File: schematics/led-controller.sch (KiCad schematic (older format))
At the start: 58 parts, among them IC1 ATMEGA168A-P, P1 CONN_01X03, P2 CONN_01X03, P3 CONN_01X02, P4 CONN_01X02, P5 CONN_01X02, P6 CONN_01X02, P7 ISP, P8 COM, Q1 IRLU 120N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

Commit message: first checked version
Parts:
- removed JP1: Jumper_NO_Small, Pin_Headers:Pin_Header_Straight_1x02, symbol Jumper_NO_Small
- added C10, C11: 100n, Capacitors_ThroughHole:C_Rect_L7_W2.5_P5, symbol C
- added CON1: BARREL_JACK, Connect:BARREL_JACK, symbol BARREL_JACK
- added D6: 1N5408, Diodes_ThroughHole:Diode_DO-201AD_Horizontal_RM15, symbol D
- added F1: 3A, Fuse_Holders_and_Fuses:Fuseholder5x20_horiz_open_lateral_Type-II, symbol FUSE
- added unit 6 of U2
- added unit 5 of U2
- C1, C2, C3, C4: footprint Capacitors_ThroughHole:C_Radial_D5_L11_P2.5 -> Capacitors_ThroughHole:C_Radial_D8_L11.5_P3.5; Order (none) -> RAD FR 100/35; Price (none) -> 0,21
- C5, C6, C7, C8, C9: Order (none) -> MKS2-100 100N; Price (none) -> 0.09
- P1: value CONN_01X03 -> VIN
- P2: value CONN_01X03 -> VOUT
- P3: value CONN_01X02 -> LED1; footprint Connect:AK300-2 -> Connect:bornier2
- P4, P5, P6: footprint Connect:AK300-2 -> Connect:bornier2
- P7: footprint Socket_Strips:Socket_Strip_Straight_2x03 -> Pin_Headers:Pin_Header_Straight_2x03
- RR4: value 20k -> 27k; Order (none) -> SIL 5-4 27; Price (none) -> 0.06
- RV1, RV2, RV3, RV4: footprint Potentiometers:Potentiometer_Trimmer-Suntan-TSR-3386C -> Trimmers:Potentiometer_Trimmer-Suntan-TSR-3296; Order (none) -> 64W-10K; Price (none) -> 0.32
- U2: footprint Housings_DIP:DIP-14_W7.62mm -> (none)
- U3: value LF33CV -> LP 2950 ACZ3,3; footprint TO_SOT_Packages_THT:TO-220_Neutral123_Vertical -> TO_SOT_Packages_THT:TO-92_Inline_Narrow_Oval; Order (none) -> LP 2950 ACZ3,3; Price (none) -> 0.33
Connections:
- net +3V3: now also P1.2 (P2), P2.2 (P2), C10.1, C11.1, U2.14 (+3V3), U2.14 (+3V3); no longer C6.1, C7.1
- net GND: now also U2.1, U2.3, C10.2, C11.2, CON1.2, CON1.3, U2.7 (GND), U2.7 (GND)
- net IRAW1: now also P3.2 (P2); no longer P3.1 (P1)
- net IRAW2: now also P4.2 (P2); no longer P4.1 (P1)
- net IRAW3: now also P5.2 (P2); no longer P5.1 (P1)
- net IRAW4: now also P6.2 (P2); no longer P6.1 (P1)
- net PULLUP1: now also RR3.3, U2.11; no longer RR3.2, U2.1
- net PULLUP2: now also RR3.2, U2.13; no longer RR3.3, U2.3
- net PULLUP3: now also RR3.5; no longer RR3.4
- net PULLUP4: now also RR3.4; no longer RR3.5
- net SENSE1: now also IC1.25 ((PCINT10/ADC2)PC2), U2.10; no longer IC1.26 ((PCINT11/ADC3)PC3), U2.2
- net SENSE2: now also IC1.26 ((PCINT11/ADC3)PC3), U2.12; no longer IC1.25 ((PCINT10/ADC2)PC2), U2.4
- net VCC: now also C6.1, C7.1, D6.1 (K)
- net at L1.1: now also P3.1 (P1); no longer P3.2 (P2)
- net at L2.1: now also P4.1 (P1); no longer P4.2 (P2)
- net at L3.1: now also P5.1 (P1); no longer P5.2 (P2)
- net at L4.1: now also P6.1 (P1); no longer P6.2 (P2)
- new net: CON1.1, F1.1
- new net: D6.2 (A), F1.2
- no-connect marks 12 -> 14
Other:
- moved on the sheet: C5, P3, P4, P5, P6, U3

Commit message: Board version 1.0 RC1
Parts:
- removed D1: 3V6, Discret:D4, symbol ZENER
- removed D6: 1N5408, Diodes_ThroughHole:Diode_DO-201AD_Horizontal_RM15, symbol D
- removed R1: 1k, Resistors_ThroughHole:Resistor_Horizontal_RM10mm, symbol R
- added C12, C13: 100n, Capacitors_ThroughHole:C_Rect_L7_W2.5_P5, symbol C
- added P9: EXPANSION, Pin_Headers:Pin_Header_Straight_1x04, symbol CONN_01X04
- added U5: 7905_wno, TO_SOT_Packages_THT:TO-92_Inline_Narrow_Oval, symbol 7905_wno
- D2, D3, D4, D5: value SD101C -> 1N5819
- P1, P2, P8: footprint Pin_Headers:Pin_Header_Straight_1x03 -> Connect:PINHEAD1-3
- R14, R15, R16: footprint Resistors_ThroughHole:Resistor_Horizontal_RM10mm -> Discret:R1
- RP1, RP2, RR1, RR2, RR3: value 10k -> 100k
- RR4: value 27k -> 4.7k; Order SIL 5-4 27 -> SIL 5-4 4,7K
- RV1, RV2, RV3, RV4: value 10k -> 1k; Order 64W-10K -> 64W-1K
- U2: footprint (none) -> Housings_DIP:DIP-14_W7.62mm
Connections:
- net +3V3: now also IC1.20 (AVCC), R14.2; no longer R14.1
- net GND: now also C13.2, U5.2 (VI)
- net ISENSE1: now also U1.4 (-); no longer U1.5 (+)
- net ISENSE2: now also U1.6 (-); no longer U1.7 (+)
- net ISENSE3: now also U1.10 (-); no longer U1.11 (+)
- net ISENSE4: now also U1.8 (-); no longer U1.9 (+)
- net REF1: now also U1.5 (+); no longer U1.4 (-)
- net REF2: now also U1.7 (+); no longer U1.6 (-)
- net REF3: now also U1.11 (+); no longer U1.10 (-)
- net REF4: now also U1.9 (+); no longer U1.8 (-)
- net RESET: now also R14.1; no longer R14.2
- net VCC: now also F1.2, C12.2, U5.1 (GND)
- net at IC1.21 (AREF): now also C13.1
- net E4: now reaches IC1.27 ((PCINT12/SDA/ADC4)PC4)
- net E4: now also P9.4 (P4)
- net E2: now reaches IC1.28 ((PCINT13/SCL/ADC5)PC5)
- net E2: now also P9.2 (P2)
- net E1: now reaches IC1.4 ((PCINT18/INT0)PD2)
- net E1: now also P9.1 (P1)
- net E3: now reaches IC1.5 ((PCINT19/OC2B/INT1)PD3)
- net E3: now also P9.3 (P3)
- net -5V: now reaches RR4.1 (COM)
- net -5V: now also C12.1, U5.3 (VO)
- no-connect marks 14 -> 8
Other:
- moved on the sheet: RP1, RR1, RR4, RV1, RV2, RV3, RV4

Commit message: Led Controller RC2
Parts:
- added C14, C15: 1u, Capacitors_ThroughHole:C_Radial_D5_L6_P2.5, symbol CP
- RP1, RP2: footprint Pin_Headers:Pin_Header_Straight_1x08 -> w_pth_resistors:r-sil_8
- RR1, RR2, RR3, RR4: footprint Pin_Headers:Pin_Header_Straight_1x05 -> w_pth_resistors:r-sil_5
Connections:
- net +3V3: now also C14.1
- net -5V: now also C15.2
- net GND: now also C14.2
- net VCC: now also C15.1
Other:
- moved on the sheet: C1, C10, C11, C2, C3, C4, C5, C6, C7, C8, C9, U3

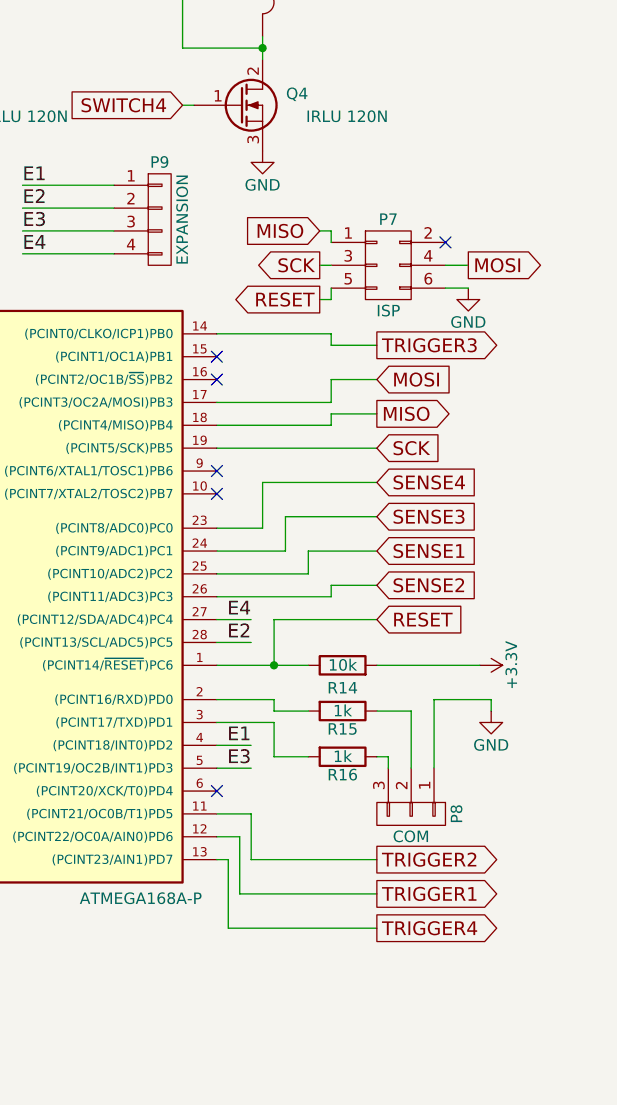
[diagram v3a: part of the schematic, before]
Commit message: RC3 -- Connected all pins to PWM outputs
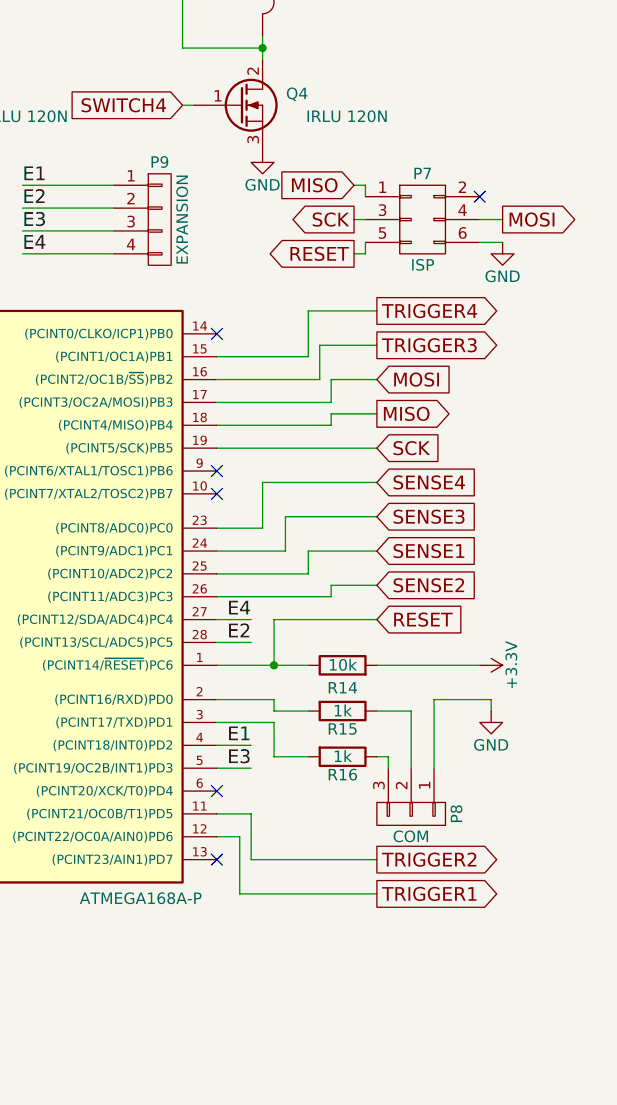
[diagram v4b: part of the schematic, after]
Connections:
- net TRIGGER3: now also IC1.16 ((PCINT2/OC1B/~SS~)PB2); no longer IC1.14 ((PCINT0/CLKO/ICP1)PB0)
- net TRIGGER4: now also IC1.15 ((PCINT1/OC1A)PB1); no longer IC1.13 ((PCINT23/AIN1)PD7)
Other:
- moved on the sheet: P7
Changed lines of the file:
@@
 Text GLabel 10400 4800 2    60   Input ~ 0
 SENSE2
-Text GLabel 10400 6300 2    60   Output ~ 0
+Text GLabel 10400 3600 2    60   Output ~ 0
 TRIGGER4
 Text GLabel 10400 6150 2    60   Output ~ 0
@@
 L CONN_02X03 P7
 U 1 1 5817965E
-P 10450 3400
-F 0 "P7" H 10450 3600 50  0000 C CNN
-F 1 "ISP" H 10450 3200 50  0000 C CNN
-F 2 "Pin_Headers:Pin_Header_Straight_2x03" H 10450 2200 50  0001 C CNN
-F 3 "" H 10450 2200 50  0000 C CNN
-	1    10450 3400
-	1    0    0    -1
-$EndComp
-Text GLabel 10150 3250 0    60   Input ~ 0
+P 10600 3200
+F 0 "P7" H 10600 3400 50  0000 C CNN
+F 1 "ISP" H 10600 3000 50  0000 C CNN
+F 2 "Pin_Headers:Pin_Header_Straight_2x03" H 10600 2000 50  0001 C CNN
+F 3 "" H 10600 2000 50  0000 C CNN
+	1    10600 3200
+	1    0    0    -1
+$EndComp
+Text GLabel 10300 3050 0    60   Input ~ 0
 MISO
-Text GLabel 10800 3400 2    60   Output ~ 0
+Text GLabel 10950 3200 2    60   Output ~ 0
 MOSI
-Text GLabel 10150 3400 0    60   Output ~ 0
+Text GLabel 10300 3200 0    60   Output ~ 0
 SCK
-Text GLabel 10150 3550 0    60   Output ~ 0
+Text GLabel 10300 3350 0    60   Output ~ 0
 RESET
 $Comp
 L GND #PWR018
 U 1 1 58179820
-P 10800 3500
-F 0 "#PWR018" H 10800 3250 50  0001 C CNN
-F 1 "GND" H 10800 3350 50  0000 C CNN
-F 2 "" H 10800 3500 50  0000 C CNN
-F 3 "" H 10800 3500 50  0000 C CNN
-	1    10800 3500
+P 10950 3300
+F 0 "#PWR018" H 10950 3050 50  0001 C CNN
+F 1 "GND" H 10950 3150 50  0000 C CNN
+F 2 "" H 10950 3300 50  0000 C CNN
+F 3 "" H 10950 3300 50  0000 C CNN
+	1    10950 3300
 	1    0    0    -1
 $EndComp
@@
 	1    0    0    -1
 $EndComp
-NoConn ~ 10700 3300
+NoConn ~ 10850 3100
 $Comp
 L VCC #PWR020
@@
 NoConn ~ 9700 4300
 NoConn ~ 9700 4400
-NoConn ~ 9700 3800
-NoConn ~ 9700 3900
 Wire Wire Line
 	1550 3800 1750 3800
@@
 Connection ~ 3450 1500
 Wire Wire Line
-	10700 3500 10800 3500
-Wire Wire Line
-	10700 3400 10800 3400
-Wire Wire Line
-	10200 3500 10200 3550
-Wire Wire Line
-	10200 3550 10150 3550
-Wire Wire Line
-	10200 3400 10150 3400
-Wire Wire Line
-	10200 3300 10200 3250
-Wire Wire Line
-	10200 3250 10150 3250
+	10850 3300 10950 3300
+Wire Wire Line
+	10850 3200 10950 3200
+Wire Wire Line
+	10350 3300 10350 3350
+Wire Wire Line
+	10350 3200 10300 3200
+Wire Wire Line
+	10350 3100 10350 3050
+Wire Wire Line
+	10350 3050 10300 3050
 Connection ~ 9950 5150
 Wire Wire Line
@@
 Connection ~ 1700 7100
 Wire Wire Line
-	10400 3750 10200 3750
-Wire Wire Line
-	10200 3750 10200 3700
-Wire Wire Line
-	10200 3700 9700 3700
+	10150 3750 10400 3750
 Wire Wire Line
 	5350 900  5800 900
@@
 Wire Wire Line
 	5400 6300 5400 6550
-Wire Wire Line
-	9700 6000 9750 6000
-Wire Wire Line
-	9750 6000 9750 6300
-Wire Wire Line
-	9750 6300 10400 6300
 Wire Wire Line
 	10400 6150 9800 6150
@@
 	5550 5200 5750 5200
 Connection ~ 5750 5200
+NoConn ~ 9700 6000
+Wire Wire Line
+	10100 3600 10400 3600
+Wire Wire Line
+	10350 3350 10300 3350
+Wire Wire Line
+	10150 3900 9700 3900
+Wire Wire Line
+	10150 3750 10150 3900
+Wire Wire Line
+	10100 3800 9700 3800
+Wire Wire Line
+	10100 3600 10100 3800
+NoConn ~ 9700 3700
 $EndSCHEMATC

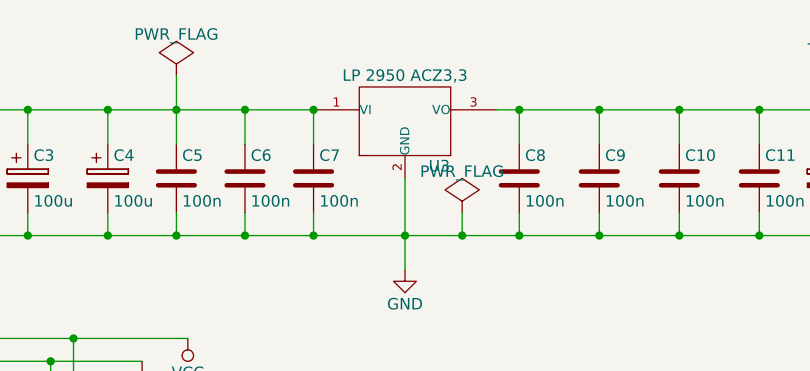
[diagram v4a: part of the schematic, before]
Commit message: Fixed small issues found on the produced board
- U3 was the wrong way round
- Holes for diodes could have been a little bigger
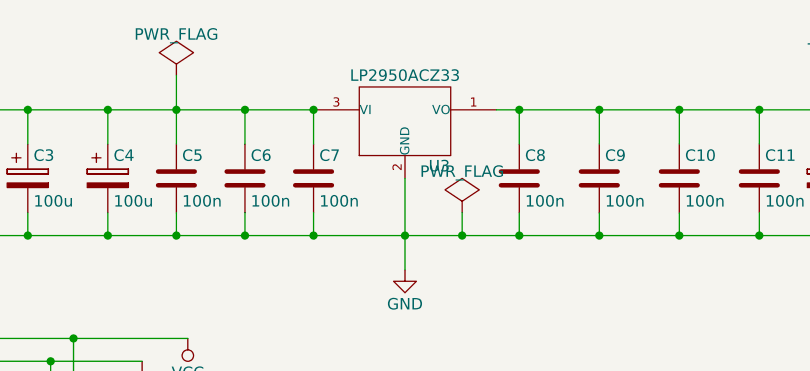
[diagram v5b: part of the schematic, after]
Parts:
- removed U3: LP 2950 ACZ3,3, TO_SOT_Packages_THT:TO-92_Inline_Narrow_Oval, symbol LF33CV
- added U3: LP2950ACZ33, TO_SOT_Packages_THT:TO-92_Inline_Narrow_Oval, symbol LP2950ACZ33
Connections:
- net +3V3: now also U3.1 (VO)
- net GND: now also U3.2 (GND)
- net VCC: now also U3.3 (VI)
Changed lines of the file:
@@
 LIBS:led-controller-resistor-networks
 LIBS:led-controller-7905
+LIBS:led-controller-lp2950-acz33
 LIBS:led-controller-cache
 EELAYER 25 0
@@
 SENSE4
 $Comp
-L LF33CV U3
-U 1 1 581223D6
-P 3200 1000
-F 0 "U3" H 3350 804 50  0000 C CNN
-F 1 "LP 2950 ACZ3,3" H 3200 1200 50  0000 C CNN
-F 2 "TO_SOT_Packages_THT:TO-92_Inline_Narrow_Oval" H 3200 1000 50  0001 C CNN
-F 3 "" H 3200 1000 50  0000 C CNN
-F 4 "LP 2950 ACZ3,3" H 3200 1000 60  0001 C CNN "Order"
-F 5 "0.33" H 3200 1000 60  0001 C CNN "Price"
-	1    3200 1000
-	1    0    0    -1
-$EndComp
-$Comp
 L GND #PWR012
 U 1 1 58122478
@@
 	10100 3600 10100 3800
 NoConn ~ 9700 3700
+$Comp
+L LP2950ACZ33 U3
+U 1 1 584D958C
+P 3200 1000
+F 0 "U3" H 3350 804 50  0000 C CNN
+F 1 "LP2950ACZ33" H 3200 1200 50  0000 C CNN
+F 2 "TO_SOT_Packages_THT:TO-92_Inline_Narrow_Oval" H 3200 1000 50  0001 C CNN
+F 3 "" H 3200 1000 50  0000 C CNN
+	1    3200 1000
+	1    0    0    -1
+$EndComp
 $EndSCHEMATC
